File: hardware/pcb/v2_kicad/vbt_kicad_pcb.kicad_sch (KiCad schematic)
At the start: 19 parts, among them J1 Conn_01x03, J2 Conn_01x04, J3 Conn_01x04, J4 Conn_01x04, SW1 SW_Push, SW2 SW_Push, U1 ESP32-WROOM-32E

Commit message: Updated Schematics for a 3/4/5/5 connection scheme to make sure items aren't plugged into the incorrect holes
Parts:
- added D1: LED, symbol Device:LED
- added R8: R, symbol Device:R
- R1: value R -> 10k
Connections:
- net GND: now also D1.1 (K); no longer C5.2, R7.1
- net VBAT_SENSE: now also C5.1, C5.2, R7.1, R7.2
- net VBAT: now reaches J4.3 (Pin_3), R6.1
- net VBAT: no longer C5.1, R7.2
- net LED: no longer names the net of U1.26 (IO4)
- net LED: now also R8.2
- new net: D1.2 (A), R8.1
- no-connect marks 23 -> 20
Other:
- moved on the sheet: C5, J4, R6, R7

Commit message: Added off_board wiring diagram and cleaned up main schematic
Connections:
- net +3V3: no longer J3.2 (Pin_2), J4.4 (Pin_4)
- net +5V: now also J2.3 (Pin_3); no longer J2.2 (Pin_2)
- net ENC_A: now also J2.1 (Pin_1); no longer J2.4 (Pin_4)
- net ENC_B: now also J2.2 (Pin_2); no longer J2.3 (Pin_3)
- net ESP_RX: now also J1.1 (Pin_1); no longer J1.3 (Pin_3)
- net GND: now also J2.4 (Pin_4), J3.3 (Pin_3); no longer C1.2, C2.2, C3.2, C4.2, J1.1 (Pin_1), J2.1 (Pin_1), J3.1 (Pin_1), SW1.1, SW2.1
- net I2C_SCL: now also J3.2 (Pin_2); no longer J3.4 (Pin_4)
- net I2C_SDA: now also J3.1 (Pin_1); no longer J3.3 (Pin_3)
- net at C3.1, R1.2: no longer SW1.2, U1.3 (EN)
- new net: C1.2, C2.2, C3.2, C4.2, SW2.1
- new net: J1.3 (Pin_3), SW1.1
- new net: SW1.2, U1.3 (EN)
- new net +3.3V: J3.4 (Pin_4), J4.4 (Pin_4)
- no-connect marks 20 -> 19
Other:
- added sheet Power_Wiring_OffBoard (offboard_power_wiring.kicad_sch)
- note added: "POWER"
- moved on the sheet: C1, C2, C3, C4, D1, J1, J2, J3, R1, R2, R3, R4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

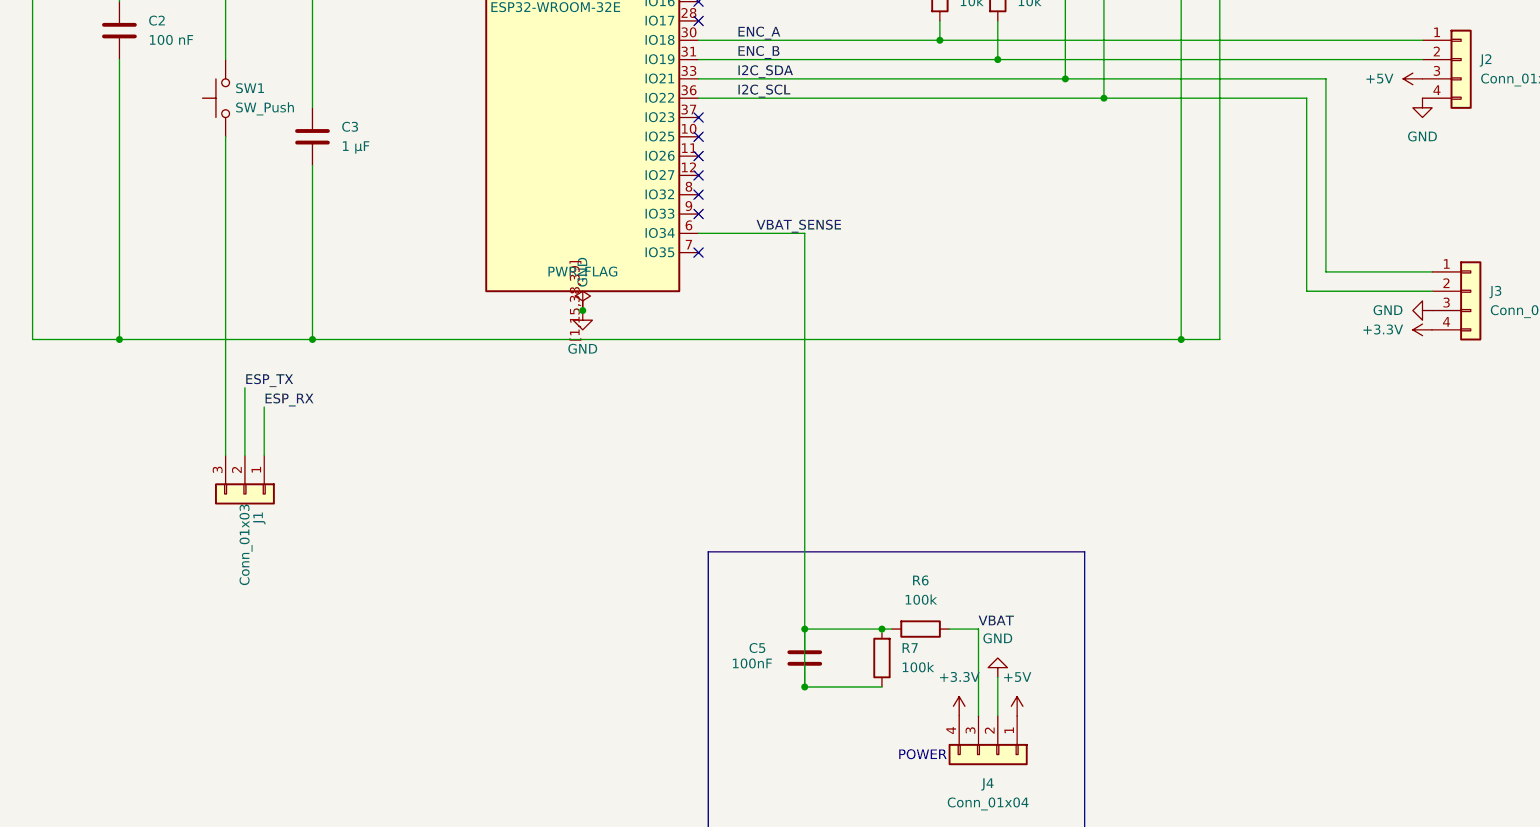
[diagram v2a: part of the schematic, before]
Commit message: updated schematics
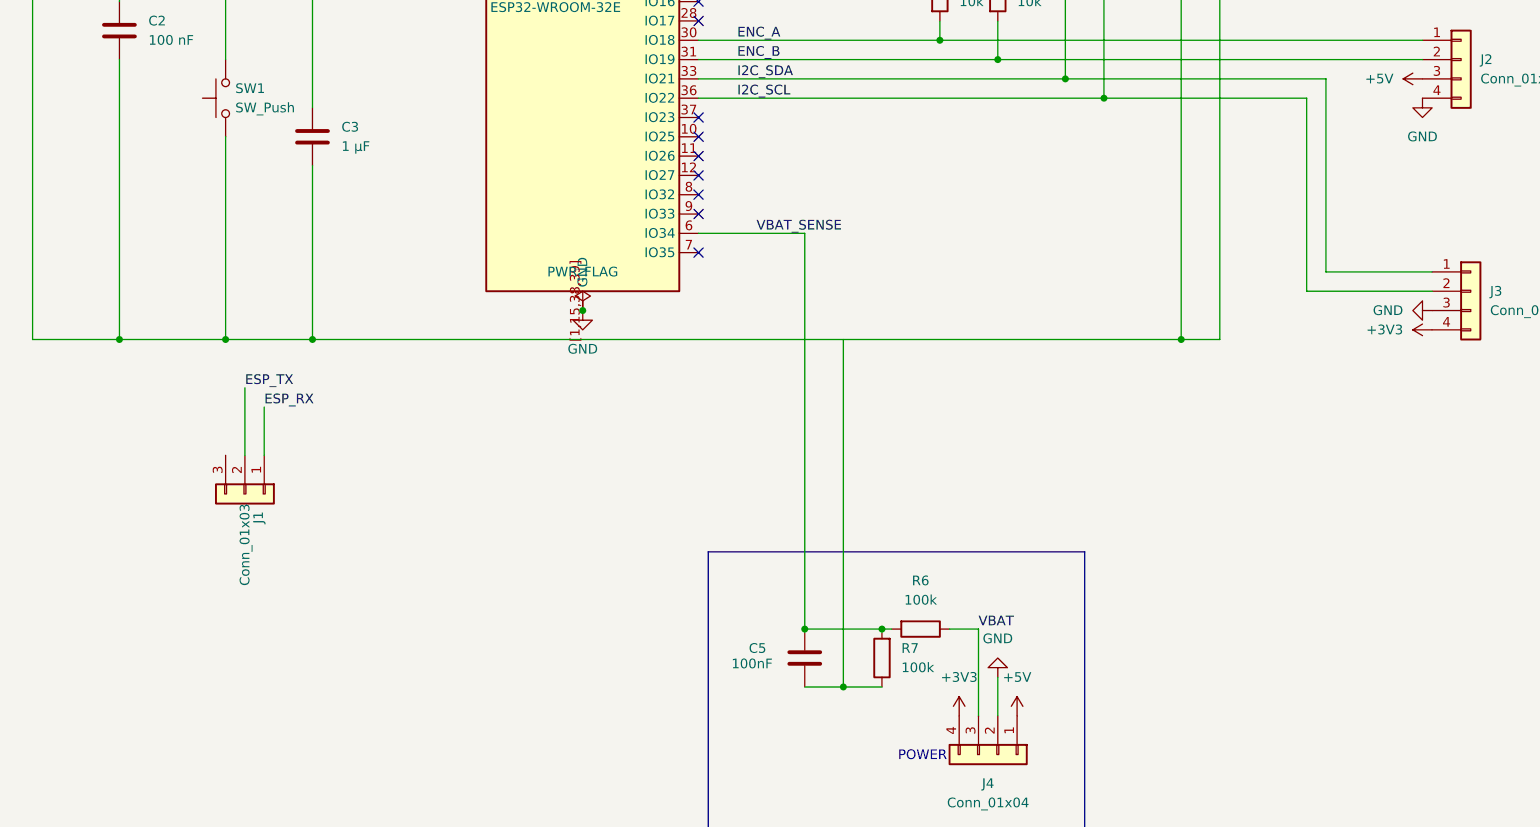
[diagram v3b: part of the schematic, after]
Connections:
- net +3.3V is gone; now on net +3V3: J3.4 (Pin_4), J4.4 (Pin_4)
- net VBAT_SENSE: no longer C5.2, R7.1
- net at C1.2, C2.2, C3.2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: now also SW1.1
- net at J1.3 (Pin_3): no longer SW1.1
- new net: C5.2, R7.1

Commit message: updated schematic
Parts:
- removed C4: 1 µF, Capacitor_SMD:C_0805_2012Metric, symbol Device:C
- R8: value R -> 330Ω
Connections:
- net ESP_RX: now also U1.34 (RXD0/IO3)
- net ESP_TX: now also U1.35 (TXD0/IO1)
- net at C1.2, C2.2, C3.2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: now also J1.3 (Pin_3)
- net at C3.1, R1.2: now also SW1.2, U1.3 (EN)
- no-connect marks 19 -> 17
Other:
- moved on the sheet: D1, J1, R8

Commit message: Updated Schematic
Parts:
- removed J2: Conn_01x04, Connector:FanPinHeader_1x04_P2.54mm_Vertical, symbol Connector_Generic:Conn_01x04
- added J2: Conn_01x05, Connector_JST:JST_XH_B5B-XH-A_1x05_P2.50mm_Vertical, symbol Connector_Generic:Conn_01x05
- C5: footprint (none) -> Capacitor_SMD:C_0805_2012Metric_Pad1.18x1.45mm_HandSolder
- J1: footprint Connector_PinSocket_2.54mm:PinSocket_1x03_P2.54mm_Vertical -> Connector_JST:JST_XH_B3B-XH-A_1x03_P2.50mm_Vertical
- J3, J4: footprint Connector:FanPinHeader_1x04_P2.54mm_Vertical -> Connector_JST:JST_XH_B4B-XH-A_1x04_P2.50mm_Vertical
- R6, R7: footprint Resistor_SMD:R_0805_2012Metric_Pad1.20x1.40mm_HandSolder -> Resistor_SMD:R_0805_2012Metric
- R8: footprint (none) -> Resistor_SMD:R_0805_2012Metric
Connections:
- net +3V3: now also J3.3 (Pin_3); no longer J3.4 (Pin_4)
- net +5V: now also J2.3 (Pin_3)
- net ENC_A: now also J2.1 (Pin_1)
- net ENC_B: now also J2.2 (Pin_2)
- net GND: now also J3.4 (Pin_4), J2.4 (Pin_4), J2.5 (Pin_5); no longer J3.3 (Pin_3)
- net I2C_SCL: now also J3.1 (Pin_1); no longer J3.2 (Pin_2)
- net I2C_SDA: now also J3.2 (Pin_2); no longer J3.1 (Pin_1)

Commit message: updated pcb schematic for finalized BOM
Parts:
- added J8: Conn_01x04, Connector_JST:JST_XH_B4B-XH-A_1x04_P2.50mm_Vertical, symbol Connector_Generic:Conn_01x04
- D1: footprint (none) -> LED_THT:LED_D5.0mm
- SW1, SW2: footprint Inductor_SMD:L_0805_2012Metric -> VBT_parts:SW_Tactile_SCHURTER_LSH_6x6mm
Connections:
- net +3V3: now also J8.3 (Pin_3)
- net ESP_RX: now also J1.2 (Pin_2); no longer J1.1 (Pin_1)
- net ESP_TX: now also J1.1 (Pin_1); no longer J1.2 (Pin_2)
- net GND: now also J8.4 (Pin_4)
- net I2C_SCL: now also J8.1 (Pin_1)
- net I2C_SDA: now also J8.2 (Pin_2)
- net at C5.2, R7.1: now also C1.2, C2.2, C3.2, J1.3 (Pin_3), SW1.1, SW2.1
